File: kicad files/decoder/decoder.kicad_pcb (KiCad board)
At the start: 2 copper layers, 102.9 x 49.5 mm, 7 parts, among them J2 Power Connector, SW1 up, SW2 down, SW3 sel

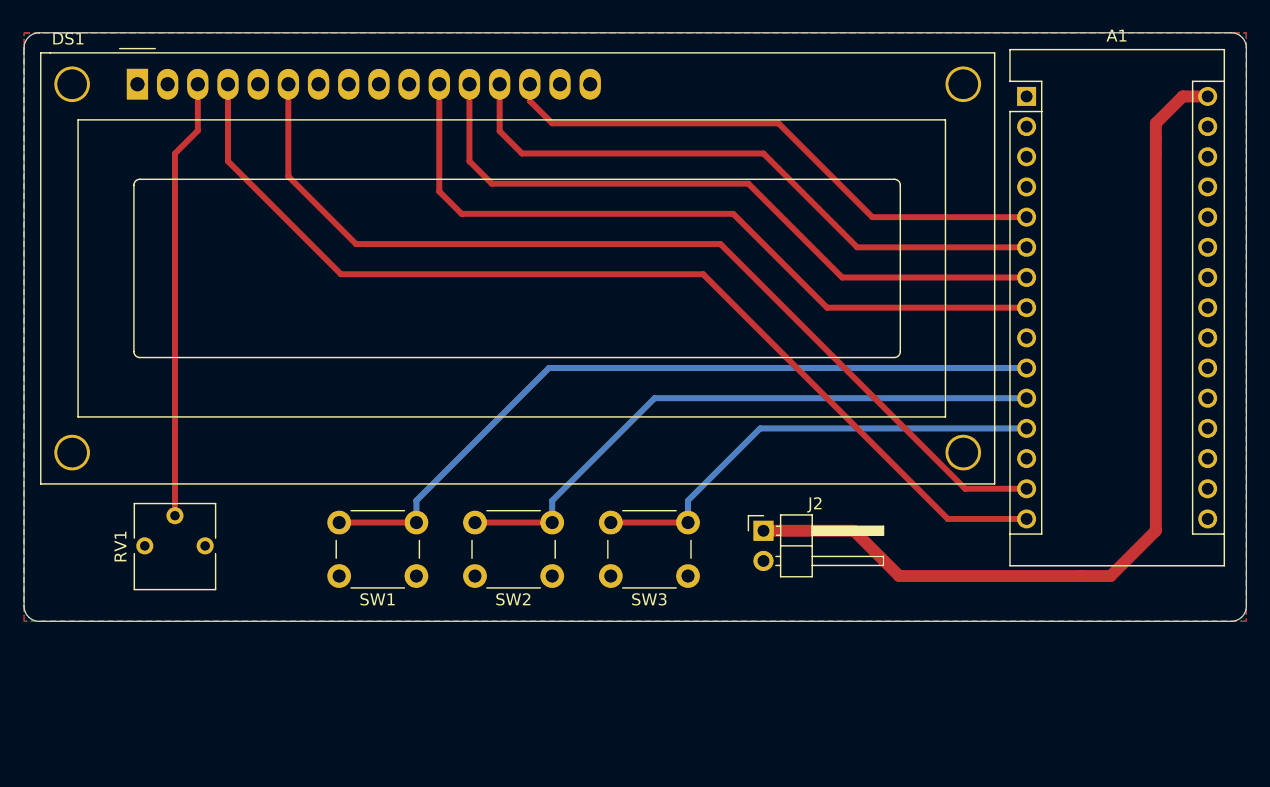
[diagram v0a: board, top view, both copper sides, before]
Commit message: added line button
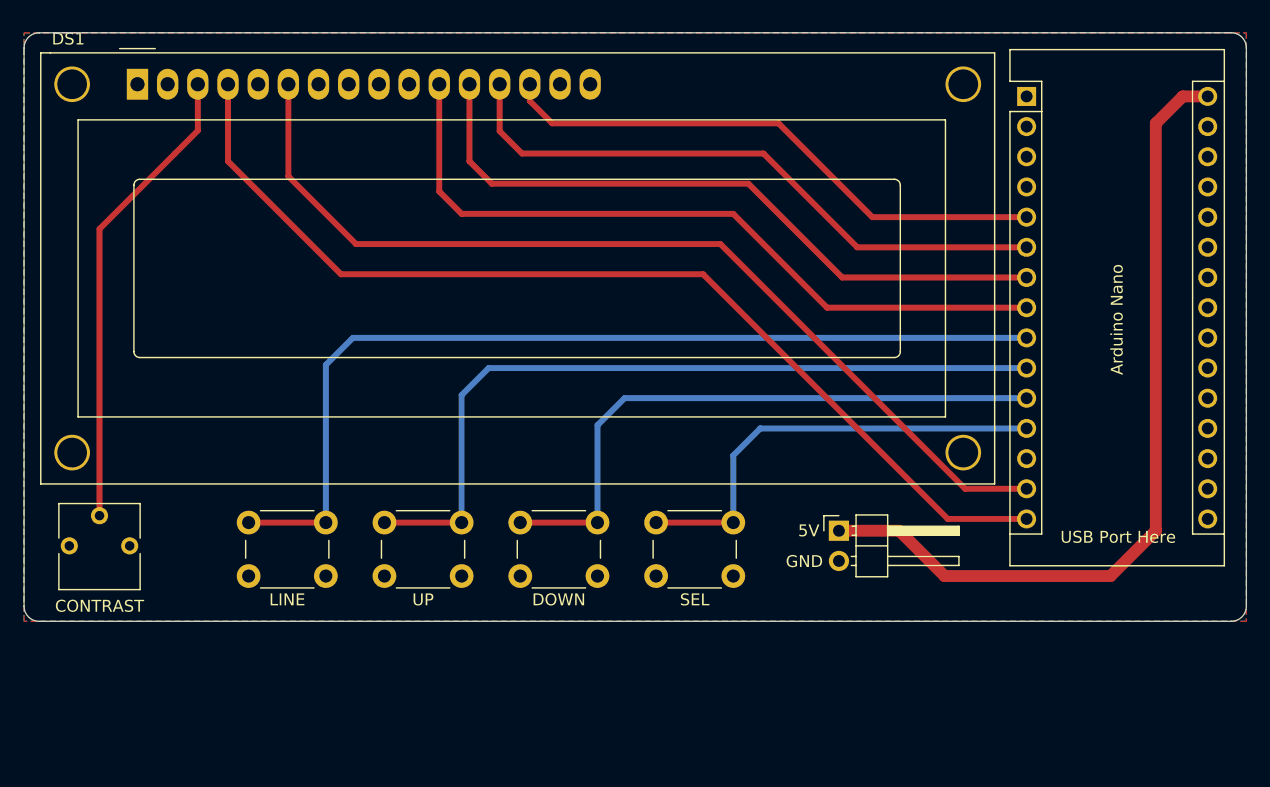
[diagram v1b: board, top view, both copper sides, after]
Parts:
- removed J2: Power Connector, Connector_PinHeader_2.54mm:PinHeader_1x02_P2.54mm_Horizontal
- added 5V: Power Connector, Connector_PinHeader_2.54mm:PinHeader_1x02_P2.54mm_Horizontal, F.Cu at (142.2, 104.1)
- added LINE: line, Button_Switch_THT:SW_PUSH_6mm, F.Cu at (99.1, 108.0)
- Arduino Nano: renamed from A1
- moved CONTRAST 6.35 mm to (82.5, 105.4)
- moved DOWN 3.81 mm to (121.9, 108.0)
- moved SEL 3.81 mm to (133.3, 108.0)
- moved UP 3.81 mm to (110.5, 108.0)
- renumbered RV1 to CONTRAST, SW2 to DOWN, SW3 to SEL, SW1 to UP
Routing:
- net Net-(A1-Pad9): track 0.00 -> 79.7 mm
- net VIN: track 75.8 -> 69.4 mm
- net Contrast: track 37.1 -> 39.7 mm
- net Net-(A1-Pad12): track 39.4 -> 37.8 mm
- net Net-(A1-Pad10): track 65.0 -> 65.7 mm
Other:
- board text added: "GND"
- board text added: "USB Port Here"

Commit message: final changes to PCB, started to clean up code on first gen PCB
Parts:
- added J1: Conn_01x01_Male, Connector_PinHeader_2.54mm:PinHeader_1x01_P2.54mm_Vertical, F.Cu at (125.7, 102.9)
- added J3: Conn_01x01_Male, Connector_PinHeader_2.54mm:PinHeader_1x01_P2.54mm_Vertical, F.Cu at (130.8, 102.9)
- added R1: 220, Resistor_THT:R_Axial_DIN0309_L9.0mm_D3.2mm_P12.70mm_Horizontal, F.Cu at (124.5, 71.1)
- A1: renamed from Arduino Nano
- moved SW4 56.1 mm to (153.7, 120.7)
- moved A1 54.7 mm to (117.8, 104.7), turned to 270 degrees
- moved RV1 48.3 mm to (130.8, 105.4)
- moved SW1 31.9 mm to (142.2, 110.5)
- moved SW2 24.0 mm to (142.2, 120.7)
- moved SW3 20.5 mm to (153.7, 110.5)
- moved J2 15.5 mm to (129.5, 113.0), turned to 270 degrees
- renumbered 5V to J2, CONTRAST to RV1, UP to SW1, DOWN to SW2, SEL to SW3, LINE to SW4
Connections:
- DS1 pad 16: GND -> Net-(DS1-Pad16)
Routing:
- net VIN: track 69.4 -> 15.6 mm
- net RS: track 86.2 -> 41.7 mm
- net Enable: track 80.8 -> 42.7 mm
- net Net-(A1-Pad12): track 37.8 -> 67.8 mm
- net D4: track 62.5 -> 41.7 mm
- net Contrast: track 39.7 -> 59.6 mm
- net Net-(A1-Pad10): track 65.7 -> 48.6 mm
- net Net-(A1-Pad9): track 79.7 -> 62.6 mm
- net D5: track 57.4 -> 41.7 mm
- net D6: track 52.3 -> 41.7 mm
- net Net-(DS1-Pad16): track 0.00 -> 5.87 mm
- net D7: track 47.3 -> 41.7 mm
- net Net-(A1-Pad11): track 51.8 -> 56.3 mm
- net +5V: track 0.00 -> 2.54 mm
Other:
- board size 102.9 x 49.5 mm -> 82.6 x 61 mm

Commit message: fixed an issue on the first rev of the PCB
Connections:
- J3 pad 1: Net-(J3-Pad1) -> GND
